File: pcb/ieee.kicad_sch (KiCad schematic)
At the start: 23 parts, among them J1 Conn_01x20_Pin, J2 Conn_01x20_Pin, J3 Screw_Terminal_01x02, J4 I2C_LCD, SW1 SW_SPST, U10 TCS34725, U11 TCS34725, U5 PCA9543AD_118, U9 D36V50F5

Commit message: Fix ERC issues and layout connectors
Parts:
- R2: renamed from R4; footprint (none) -> Resistor_THT:R_Axial_DIN0309_L9.0mm_D3.2mm_P15.24mm_Horizontal
- R4: renamed from R3; footprint (none) -> Resistor_THT:R_Axial_DIN0309_L9.0mm_D3.2mm_P15.24mm_Horizontal
- renumbered A3 to A2, J3 to J1, J1 to J2, J2 to J3, R2 to R1, R1 to R3, U11 to U1, U5 to U2, U9 to U3, U10 to U4
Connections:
- net +3V3: now also R2.1, R4.2

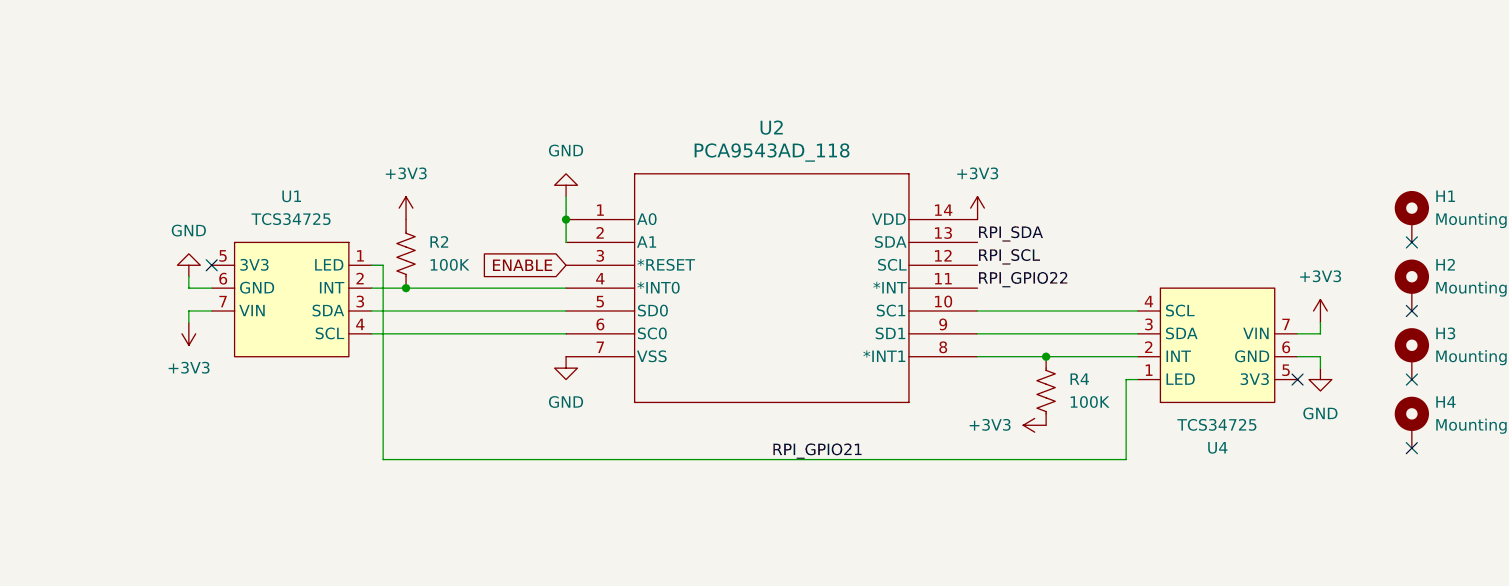
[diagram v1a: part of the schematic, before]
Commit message: Route I2C and planes
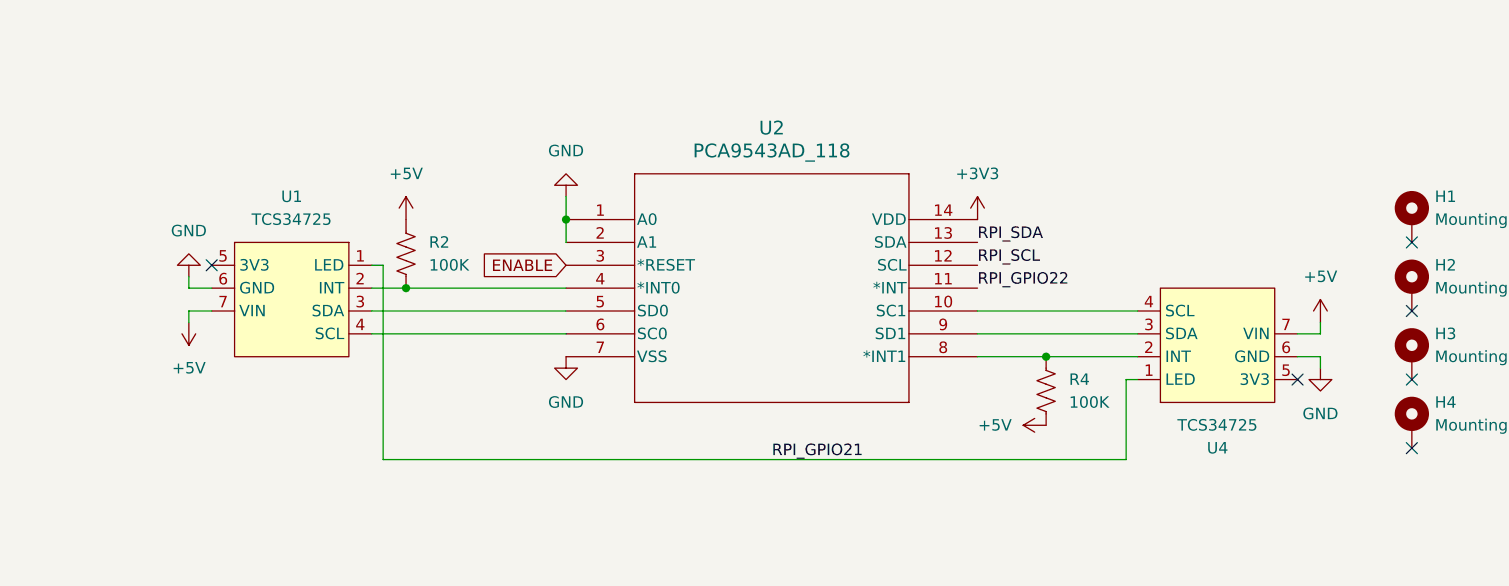
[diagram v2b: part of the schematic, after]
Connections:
- net +3V3: no longer R2.1, R4.2, U1.7 (VIN), U4.7 (VIN)
- net +5V: now also R2.1, R4.2, U1.7 (VIN), U4.7 (VIN)
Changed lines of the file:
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@@
 			)
 		)
-		(property "Value" "+3V3"
+		(property "Value" "+5V"
 			(at 214.63 157.4799 90)
 			(effects
@@
 			)
 		)
-		(property "Value" "+3V3"
+		(property "Value" "+5V"
 			(at 147.32 129.54 0)
 			(effects
@@
 			)
 		)
-		(property "Value" "+3V3"
+		(property "Value" "+5V"
 			(at 123.19 151.13 0)
 			(effects
@@
 			)
 		)
-		(property "Value" "+3V3"
+		(property "Value" "+5V"
 			(at 248.92 140.97 0)
 			(effects

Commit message: Finish layout
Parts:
- removed H2: MountingHole_Pad, MountingHole:MountingHole_3.2mm_M3_Pad, symbol Mechanical:MountingHole_Pad
- added C6, C7: 0.1uF, Capacitor_SMD:C_0603_1608Metric_Pad1.08x0.95mm_HandSolder, symbol Device:C
- added C8: 1uF, Capacitor_SMD:C_0603_1608Metric_Pad1.08x0.95mm_HandSolder, symbol Device:C
- renumbered H3 to H2, H4 to H3
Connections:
- net +3V3: now also C7.2
- net +5V: now also C6.2, C8.2
- net GND: now also C6.1, C7.1, C8.1
- net RPI_GPIO17: now also U2.11 (*INT)
- net RPI_GPIO21: now also SW1.1 (A); no longer U1.1 (LED), U4.1 (LED)
- net RPI_GPIO22: no longer U2.11 (*INT)
- net RPI_GPIO26: no longer SW1.1 (A)
- net RPI_GPIO4: now also U1.1 (LED), U4.1 (LED)
- net manipulation/CRANK_PWM1: now also JP2.1 (A), JP4.1 (A); no longer JP1.1 (A), JP3.1 (A)
- net manipulation/CRANK_PWM2: now also JP1.1 (A), JP3.1 (A); no longer JP2.1 (A), JP4.1 (A)
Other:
- moved on the sheet: J2, J3
